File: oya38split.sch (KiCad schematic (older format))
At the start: 46 parts, among them M12 MX-NoLED, U1 ProMicro

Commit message: fixed schematics
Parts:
- added D? (x10): D_Small, symbol Device:D_Small
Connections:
- new net: D?.2 (A), MX39.2 (ROW)
- new net: D?.2 (A), MX40.2 (ROW)
- new net: D?.2 (A), MX41.2 (ROW)
- new net: D?.2 (A), MX42.2 (ROW)
- new net: D?.2 (A), MX43.2 (ROW)
- new net: D?.2 (A), MX1.2 (ROW)
- new net: D?.2 (A), MX2.2 (ROW)
- new net: D?.2 (A), MX3.2 (ROW)
- new net: D?.2 (A), MX4.2 (ROW)
- new net: D?.2 (A), MX5.2 (ROW)
- now unconnected: M12.1 (COL), M12.2 (ROW), MX1.1 (COL), MX10.1 (COL), MX10.2 (ROW), MX11.1 (COL), MX11.2 (ROW), MX13.1 (COL), MX13.2 (ROW), MX14.1 (COL), MX14.2 (ROW), MX15.1 (COL), MX15.2 (ROW), MX16.1 (COL), MX16.2 (ROW), MX17.1 (COL), MX17.2 (ROW), MX18.1 (COL), MX18.2 (ROW), MX19.1 (COL), MX19.2 (ROW), MX2.1 (COL), MX20.1 (COL), MX20.2 (ROW), MX21.1 (COL), MX21.2 (ROW), MX22.1 (COL), MX22.2 (ROW), MX23.1 (COL), MX23.2 (ROW), MX24.1 (COL), MX24.2 (ROW), MX25.1 (COL), MX25.2 (ROW), MX26.1 (COL), MX26.2 (ROW), MX27.1 (COL), MX27.2 (ROW), MX28.1 (COL), MX28.2 (ROW), MX29.1 (COL), MX29.2 (ROW), MX3.1 (COL), MX30.1 (COL), MX30.2 (ROW), MX31.1 (COL), MX31.2 (ROW), MX32.1 (COL), MX32.2 (ROW), MX33.1 (COL), MX33.2 (ROW), MX34.1 (COL), MX34.2 (ROW), MX35.1 (COL), MX35.2 (ROW), MX36.1 (COL), MX36.2 (ROW), MX37.1 (COL), MX37.2 (ROW), MX38.1 (COL), MX38.2 (ROW), MX39.1 (COL), MX4.1 (COL), MX40.1 (COL), MX41.1 (COL), MX42.1 (COL), MX43.1 (COL), MX44.1 (COL), MX44.2 (ROW), MX45.1 (COL), MX45.2 (ROW), MX5.1 (COL), MX6.1 (COL), MX6.2 (ROW), MX7.1 (COL), MX7.2 (ROW), MX8.1 (COL), MX8.2 (ROW), MX9.1 (COL), MX9.2 (ROW)
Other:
- moved on the sheet: M12, MX11, MX13, MX14, MX15, MX16, MX17, MX18, MX19, MX20, MX21, MX22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

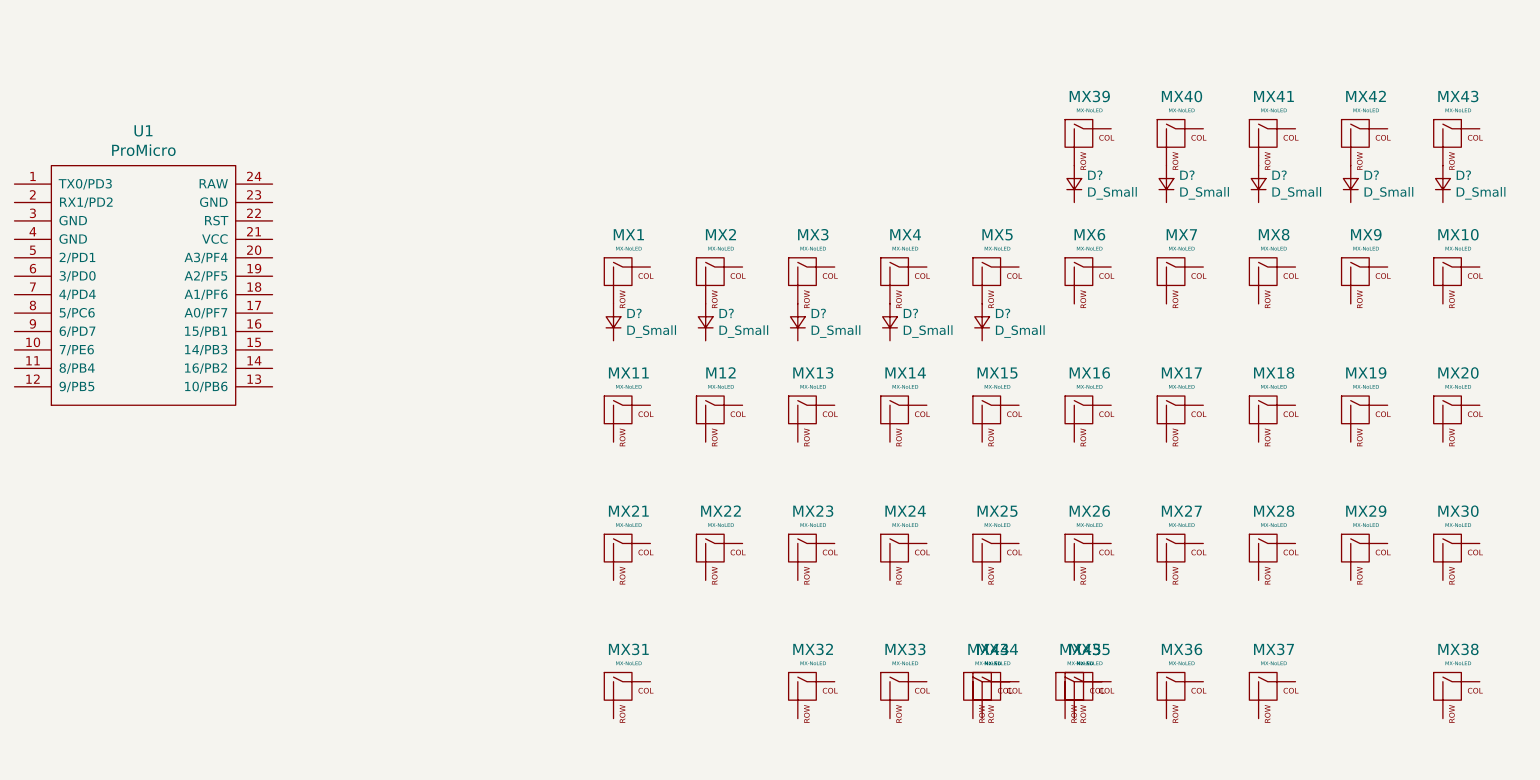
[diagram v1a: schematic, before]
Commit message: named diodes
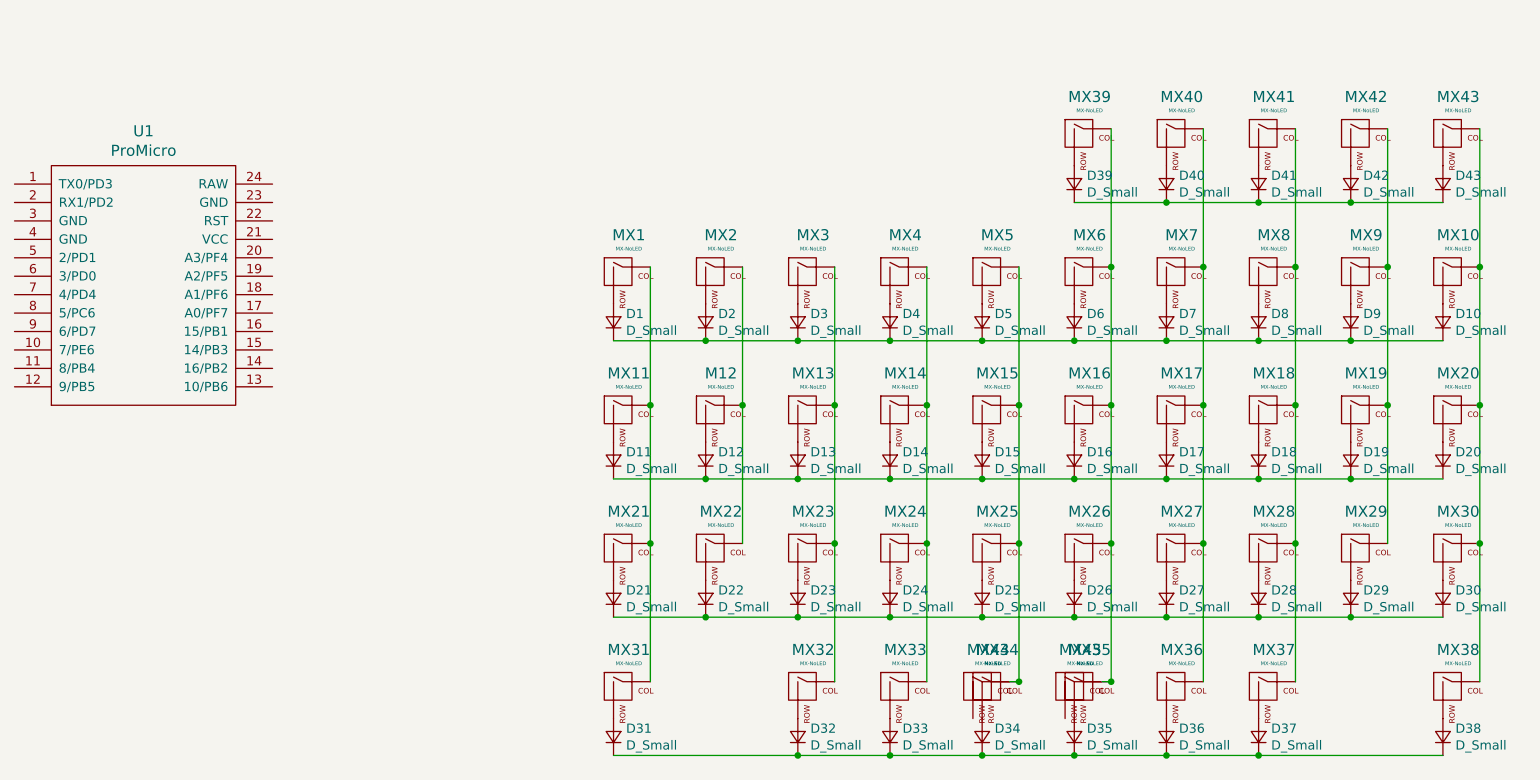
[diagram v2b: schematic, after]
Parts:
- added D10, D11, D12, D13, D14, D15, D16, D17, D18, D19, D20, D21, D22, D23, D24, D25, D26, D27, D28, D29, D30, D31, D32, D33, D34, D35, D36, D37, D38, D6, D7, D8, D9: D_Small, symbol Device:D_Small
- gave numbers to parts that had none: 10
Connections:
- net at MX39.1 (COL): now also MX16.1 (COL), MX26.1 (COL), MX35.1 (COL), MX45.1 (COL), MX6.1 (COL)
- net at MX40.1 (COL): now also MX17.1 (COL), MX27.1 (COL), MX36.1 (COL), MX7.1 (COL)
- net at MX41.1 (COL): now also MX18.1 (COL), MX28.1 (COL), MX37.1 (COL), MX8.1 (COL)
- net at MX42.1 (COL): now also MX19.1 (COL), MX29.1 (COL), MX9.1 (COL)
- net at MX43.1 (COL): now also MX10.1 (COL), MX20.1 (COL), MX30.1 (COL), MX38.1 (COL)
- net at MX1.1 (COL): now also MX11.1 (COL), MX21.1 (COL), MX31.1 (COL)
- net at MX2.1 (COL): now also M12.1 (COL), MX22.1 (COL)
- net at MX3.1 (COL): now also MX13.1 (COL), MX23.1 (COL), MX32.1 (COL)
- net at MX4.1 (COL): now also MX14.1 (COL), MX24.1 (COL), MX33.1 (COL)
- net at MX5.1 (COL): now also MX15.1 (COL), MX25.1 (COL), MX34.1 (COL), MX44.1 (COL)
- net at MX6.2 (ROW): now also D6.2 (A)
- net at MX7.2 (ROW): now also D7.2 (A)
- net at MX8.2 (ROW): now also D8.2 (A)
- net at MX9.2 (ROW): now also D9.2 (A)
- net at MX10.2 (ROW): now also D10.2 (A)
- net at MX11.2 (ROW): now also D11.2 (A)
- net at M12.2 (ROW): now also D12.2 (A)
- net at MX13.2 (ROW): now also D13.2 (A)
- net at MX14.2 (ROW): now also D14.2 (A)
- net at MX15.2 (ROW): now also D15.2 (A)
- net at MX16.2 (ROW): now also D16.2 (A)
- net at MX17.2 (ROW): now also D17.2 (A)
- net at MX18.2 (ROW): now also D18.2 (A)
- net at MX19.2 (ROW): now also D19.2 (A)
- net at MX20.2 (ROW): now also D20.2 (A)
- net at MX21.2 (ROW): now also D21.2 (A)
- net at MX22.2 (ROW): now also D22.2 (A)
- net at MX23.2 (ROW): now also D23.2 (A)
- net at MX24.2 (ROW): now also D24.2 (A)
- net at MX25.2 (ROW): now also D25.2 (A)
- net at MX26.2 (ROW): now also D26.2 (A)
- net at MX27.2 (ROW): now also D27.2 (A)
- net at MX28.2 (ROW): now also D28.2 (A)
- net at MX29.2 (ROW): now also D29.2 (A)
- net at MX30.2 (ROW): now also D30.2 (A)
- net at MX31.2 (ROW): now also D31.2 (A)
- net at MX33.2 (ROW): now also D33.2 (A)
- net at MX34.2 (ROW): now also D34.2 (A)
- net at MX35.2 (ROW): now also D35.2 (A)
- net at MX36.2 (ROW): now also D36.2 (A)
- net at MX38.2 (ROW): now also D38.2 (A)
- net at MX32.2 (ROW): now also D32.2 (A)
- net at MX37.2 (ROW): now also D37.2 (A)
- net at D39.1 (K): now also D40.1 (K), D41.1 (K), D42.1 (K), D43.1 (K)
- net at D1.1 (K): now also D2.1 (K), D3.1 (K), D4.1 (K), D5.1 (K), D10.1 (K), D6.1 (K), D7.1 (K), D8.1 (K), D9.1 (K)
- new net: D11.1 (K), D12.1 (K), D13.1 (K), D14.1 (K), D15.1 (K), D16.1 (K), D17.1 (K), D18.1 (K), D19.1 (K), D20.1 (K)
- new net: D21.1 (K), D22.1 (K), D23.1 (K), D24.1 (K), D25.1 (K), D26.1 (K), D27.1 (K), D28.1 (K), D29.1 (K), D30.1 (K)
- new net: D31.1 (K), D32.1 (K), D33.1 (K), D34.1 (K), D35.1 (K), D36.1 (K), D37.1 (K), D38.1 (K)

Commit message: added some of the schematics
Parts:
- D1, D10, D11, D12, D13, D14, D15, D16, D17, D18, D19, D2, D20, D21, D22, D23, D24, D25, D26, D27, D28, D29, D3, D30, D31, D32, D33, D34, D35, D36, D37, D38, D39, D4, D40, D41, D42, D43, D5, D6, D7, D8, D9: footprint (none) -> Diode_SMD:D_SOD-123
- M12, MX1, MX10, MX11, MX13, MX14, MX15, MX16, MX17, MX18, MX19, MX2, MX20, MX21, MX22, MX23, MX24, MX25, MX26, MX27, MX28, MX29, MX3, MX30, MX31, MX32, MX33, MX34, MX35, MX36, MX37, MX38, MX39, MX4, MX40, MX41, MX42, MX43, MX44, MX45, MX5, MX6, MX7, MX8, MX9: footprint (none) -> MX_Only:MXOnly-1U-NoLED

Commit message: added sch to pcb
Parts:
- D1, D10, D11, D12, D13, D14, D15, D16, D17, D18, D19, D2, D20, D21, D22, D23, D24, D25, D26, D27, D28, D29, D3, D30, D31, D32, D33, D34, D35, D36, D37, D38, D39, D4, D40, D41, D42, D43, D5, D6, D7, D8, D9: footprint Diode_SMD:D_SOD-123 -> kbd:D3_SMD_v2
- MX44, MX45: footprint MX_Only:MXOnly-1U-NoLED -> MX_Only:MXOnly-2U-ReversedStabilizers-NoLED
- U1: footprint (none) -> Keebio-Parts:ArduinoProMicro

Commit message: layout
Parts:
- renumbered M12 to MX12
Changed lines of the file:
@@
-$EndComp
-$Comp
-L MX_Alps_Hybrid:MX-NoLED M12
-U 1 1 6140893D
-P 6100 3850
-F 0 "M12" H 6133 4073 60  0000 C CNN
-F 1 "MX-NoLED" H 6133 3999 20  0000 C CNN
-F 2 "MX_Only:MXOnly-1U-NoLED" H 5475 3825 60  0001 C CNN
-F 3 "" H 5475 3825 60  0001 C CNN
-	1    6100 3850
-	1    0    0    -1
 $EndComp
 $Comp
@@
 	5750 4550 5750 5300
 Wire Wire Line
-	6250 3050 6250 3800
-Connection ~ 6250 3800
-Wire Wire Line
-	6250 3800 6250 4550
-Wire Wire Line
 	6750 3050 6750 3800
 Connection ~ 6750 3800
@@
 	0    -1   -1   0
 $EndComp
+Connection ~ 6250 3800
+Wire Wire Line
+	6250 3800 6250 4550
+Wire Wire Line
+	6250 3050 6250 3800
+$Comp
+L MX_Alps_Hybrid:MX-NoLED MX12
+U 1 1 6140893D
+P 6100 3850
+F 0 "MX12" H 6133 4073 60  0000 C CNN
+F 1 "MX-NoLED" H 6133 3999 20  0000 C CNN
+F 2 "MX_Only:MXOnly-1U-NoLED" H 5475 3825 60  0001 C CNN
+F 3 "" H 5475 3825 60  0001 C CNN
+	1    6100 3850
+	1    0    0    -1
+$EndComp
 $EndSCHEMATC

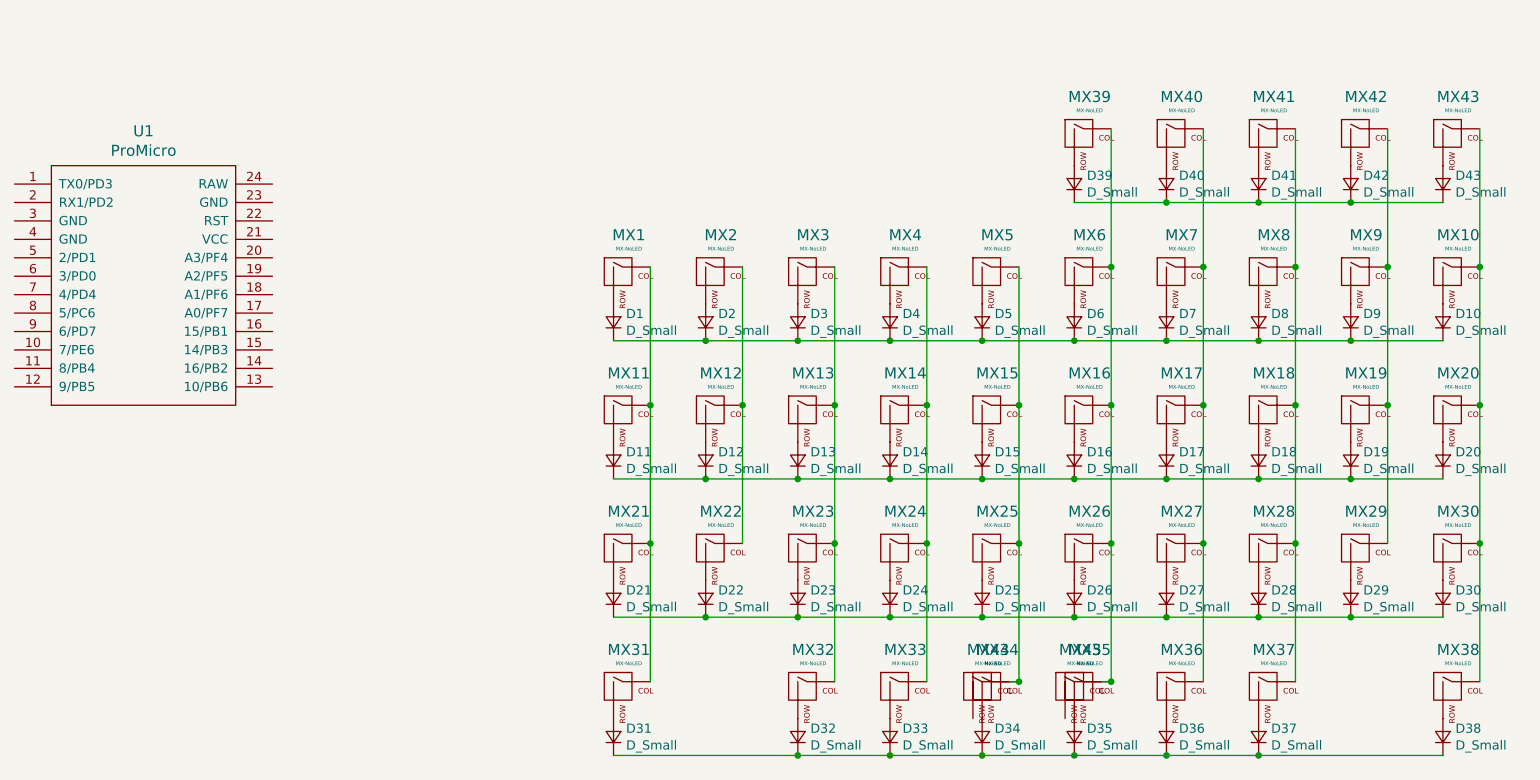
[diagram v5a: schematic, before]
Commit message: named col and rows
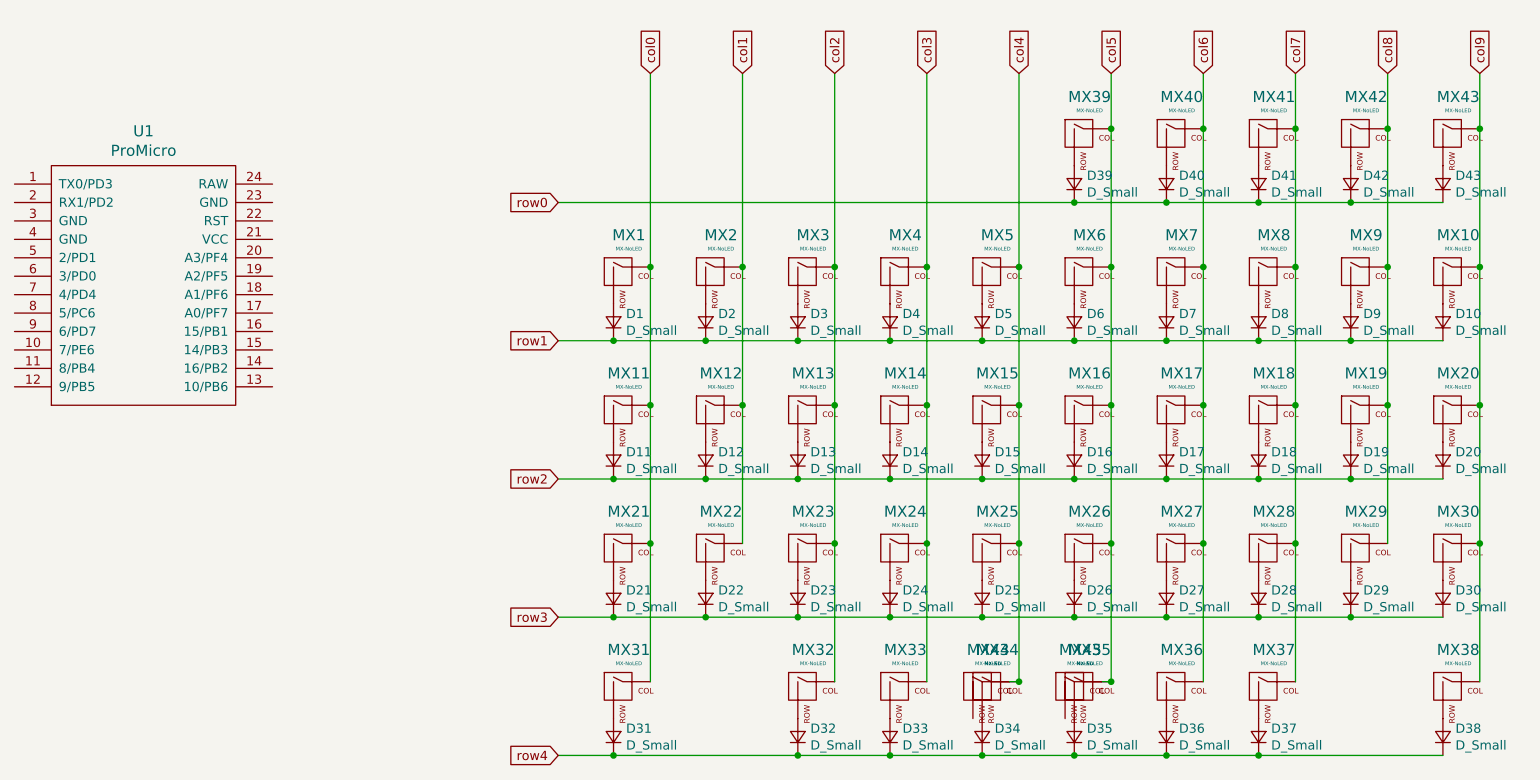
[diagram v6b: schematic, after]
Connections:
- net col5: now reaches MX16.1 (COL), MX26.1 (COL), MX35.1 (COL), MX39.1 (COL), MX45.1 (COL), MX6.1 (COL)
- net col6: now reaches MX17.1 (COL), MX27.1 (COL), MX36.1 (COL), MX40.1 (COL), MX7.1 (COL)
- net col7: now reaches MX18.1 (COL), MX28.1 (COL), MX37.1 (COL), MX41.1 (COL), MX8.1 (COL)
- net col8: now reaches MX19.1 (COL), MX29.1 (COL), MX42.1 (COL), MX9.1 (COL)
- net col9: now reaches MX10.1 (COL), MX20.1 (COL), MX30.1 (COL), MX38.1 (COL), MX43.1 (COL)
- net col0: now reaches MX1.1 (COL), MX11.1 (COL), MX21.1 (COL), MX31.1 (COL)
- net col1: now reaches MX12.1 (COL), MX2.1 (COL), MX22.1 (COL)
- net col2: now reaches MX13.1 (COL), MX23.1 (COL), MX3.1 (COL), MX32.1 (COL)
- net col3: now reaches MX14.1 (COL), MX24.1 (COL), MX33.1 (COL), MX4.1 (COL)
- net col4: now reaches MX15.1 (COL), MX25.1 (COL), MX34.1 (COL), MX44.1 (COL), MX5.1 (COL)
- net row0: now reaches D39.1 (K), D40.1 (K), D41.1 (K), D42.1 (K), D43.1 (K)
- net row1: now reaches D1.1 (K), D10.1 (K), D2.1 (K), D3.1 (K), D4.1 (K), D5.1 (K), D6.1 (K), D7.1 (K), D8.1 (K), D9.1 (K)
- net row2: now reaches D11.1 (K), D12.1 (K), D13.1 (K), D14.1 (K), D15.1 (K), D16.1 (K), D17.1 (K), D18.1 (K), D19.1 (K), D20.1 (K)
- net row3: now reaches D21.1 (K), D22.1 (K), D23.1 (K), D24.1 (K), D25.1 (K), D26.1 (K), D27.1 (K), D28.1 (K), D29.1 (K), D30.1 (K)
- net row4: now reaches D31.1 (K), D32.1 (K), D33.1 (K), D34.1 (K), D35.1 (K), D36.1 (K), D37.1 (K), D38.1 (K)
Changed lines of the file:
@@
 	1    0    0    -1
 $EndComp
+Wire Wire Line
+	10250 2300 10250 2000
+Connection ~ 10250 2300
+Wire Wire Line
+	9750 2300 9750 2000
+Connection ~ 9750 2300
+Wire Wire Line
+	9250 2300 9250 2000
+Connection ~ 9250 2300
+Wire Wire Line
+	8750 2300 8750 2000
+Connection ~ 8750 2300
+Wire Wire Line
+	8250 2300 8250 2000
+Connection ~ 8250 2300
+Wire Wire Line
+	5550 3450 5250 3450
+Connection ~ 5550 3450
+Wire Wire Line
+	5550 4200 5250 4200
+Connection ~ 5550 4200
+Wire Wire Line
+	5550 4950 5250 4950
+Connection ~ 5550 4950
+Wire Wire Line
+	5550 5700 5250 5700
+Connection ~ 5550 5700
+Wire Wire Line
+	7750 3050 7750 2000
+Connection ~ 7750 3050
+Wire Wire Line
+	7250 3050 7250 2000
+Connection ~ 7250 3050
+Wire Wire Line
+	6750 3050 6750 2000
+Connection ~ 6750 3050
+Wire Wire Line
+	6250 3050 6250 2000
+Connection ~ 6250 3050
+Wire Wire Line
+	5750 3050 5750 2000
+Connection ~ 5750 3050
+Wire Wire Line
+	8050 2700 5250 2700
+Connection ~ 8050 2700
+Text GLabel 5750 2000 1    50   Input ~ 0
+col0
+Text GLabel 6250 2000 1    50   Input ~ 0
+col1
+Text GLabel 6750 2000 1    50   Input ~ 0
+col2
+Text GLabel 7250 2000 1    50   Input ~ 0
+col3
+Text GLabel 7750 2000 1    50   Input ~ 0
+col4
+Text GLabel 8250 2000 1    50   Input ~ 0
+col5
+Text GLabel 8750 2000 1    50   Input ~ 0
+col6
+Text GLabel 9250 2000 1    50   Input ~ 0
+col7
+Text GLabel 9750 2000 1    50   Input ~ 0
+col8
+Text GLabel 10250 2000 1    50   Input ~ 0
+col9
+Text GLabel 5250 2700 0    50   Input ~ 0
+row0
+Text GLabel 5250 3450 0    50   Input ~ 0
+row1
+Text GLabel 5250 4200 0    50   Input ~ 0
+row2
+Text GLabel 5250 4950 0    50   Input ~ 0
+row3
+Text GLabel 5250 5700 0    50   Input ~ 0
+row4
 $EndSCHEMATC
